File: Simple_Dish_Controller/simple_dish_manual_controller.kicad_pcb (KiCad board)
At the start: 4 copper layers, 65 x 75 mm, 50 parts, among them J1 Screw_Terminal_01x02, J2 Conn_01x02_Pin, J3 Screw Terminal To Chassis, J4 Conn_01x03_Pin, J5 Elevation DE-15, J6 Conn_01x03_Pin, J7 Azimuth DE-15, Q1 MMBT2222A, Q2 MMBT2222A, Q3 MMBT2222A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

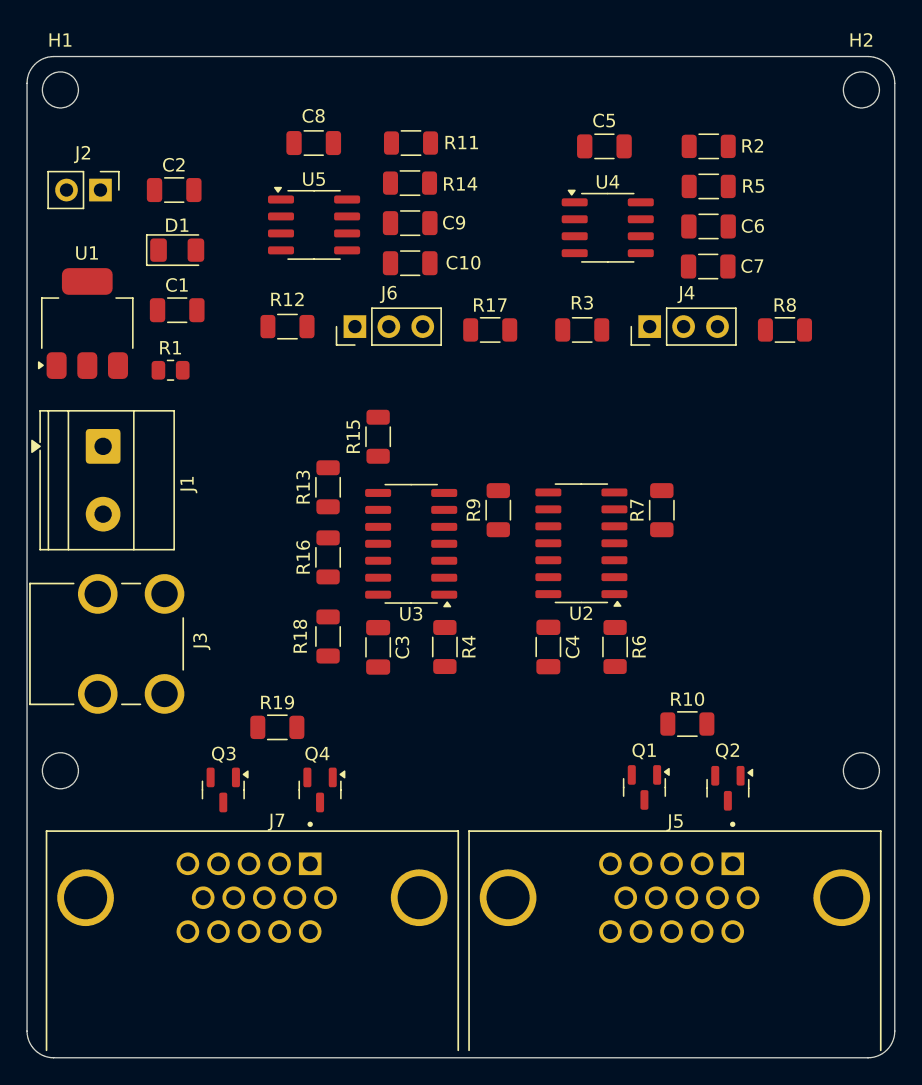
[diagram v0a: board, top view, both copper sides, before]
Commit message: Component placement and added traces
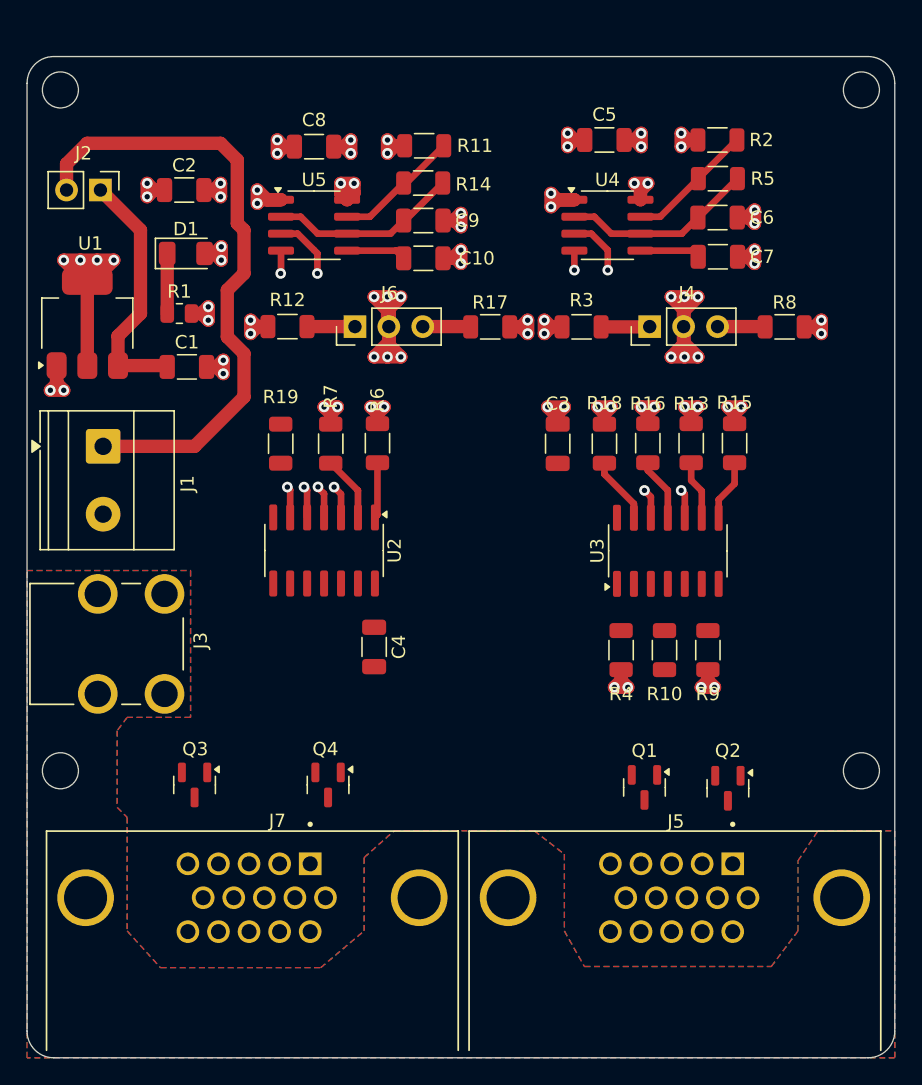
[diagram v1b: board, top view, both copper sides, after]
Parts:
- moved R13 27.4 mm to (220.2, 76.4)
- moved R15 26.7 mm to (223.5, 76.4)
- moved R16 25.4 mm to (217.0, 76.4)
- moved R7 25.3 mm to (193.2, 76.4)
- moved R18 25.2 mm to (213.8, 76.4), turned to 90 degrees
- moved R6 23.5 mm to (196.8, 76.4), turned to 90 degrees
- moved R19 21.3 mm to (189.5, 76.4), turned to -90 degrees
- moved C3 20.3 mm to (210.2, 76.4), turned to 90 degrees
- moved U2 19.3 mm to (192.8, 84.4), turned to -90 degrees
- moved U3 19.2 mm to (218.5, 84.4), turned to 90 degrees
- moved R9 18.9 mm to (221.5, 91.9), turned to -90 degrees
- moved R4 13.2 mm to (215.0, 91.9)
- moved C4 13.1 mm to (196.5, 91.6)
- moved R10 5.80 mm to (218.2, 91.9), turned to -90 degrees
- moved C1 4.31 mm to (182.5, 70.7)
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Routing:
- net GND: track 0.00 -> 89.8 mm, vias 0 -> 50
- net +5V: track 0.00 -> 84.8 mm, vias 0 -> 32
- net /IN_5VDC: track 0.00 -> 47.0 mm
- net /IN_5VDC_SWITCH: track 0.00 -> 18.8 mm
- net Net-(U4-THR): track 0.00 -> 14.4 mm
- net Net-(U5-THR): track 0.00 -> 14.2 mm
- net Net-(U4-DIS): track 0.00 -> 9.61 mm
- net Net-(U5-DIS): track 0.00 -> 9.44 mm
- net Net-(J6-Pin_3): track 0.00 -> 8.60 mm
- net Net-(R15-Pad1): track 0.00 -> 7.15 mm, vias 0 -> 1
- net Net-(R16-Pad1): track 0.00 -> 7.12 mm, vias 0 -> 1
- net /Azimuth/Dir Sig: track 0.00 -> 6.11 mm, vias 0 -> 1
- net Net-(R7-Pad1): track 0.00 -> 4.91 mm
- net /Azimuth/Pul sig: track 0.00 -> 4.84 mm, vias 0 -> 1
- net Net-(U4-CV): track 0.00 -> 4.52 mm
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- added copper zone on B.Cu, net Shield
- added copper zone on F.Cu, net Shield
- added copper zone on In1.Cu, net Shield
- added copper zone on In2.Cu, net Shield
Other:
- board text added: "25/04/2025"
- board text added: "DISH CONTROLLER"
- board text added: "HW 1.0.0"

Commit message: Final version of the PCB.Production files were generated in -Production- folder
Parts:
- C3, C4, C5, C8: value 0.1uF -> 100nF
- R1: footprint Resistor_SMD:R_0805_2012Metric -> Resistor_SMD:R_1206_3216Metric
- moved U3 5.21 mm to (213.3, 84.4)
- moved R10 4.94 mm to (213.3, 92.5)
- moved R4 4.94 mm to (210.1, 92.5)
- moved R9 4.94 mm to (216.6, 92.5)
- moved C3 3.55 mm to (206.7, 76.4)
- moved R13 3.55 mm to (216.7, 76.4)
- moved R15 3.55 mm to (219.9, 76.4)
- moved R16 3.55 mm to (213.4, 76.4)
- moved R18 3.55 mm to (210.2, 76.4)
- moved Q1 2.95 mm to (213.8, 102.2)
- moved Q2 1.30 mm to (224.3, 102.2)
- moved Q3 0.97 mm to (182.1, 102.2)
- moved C4 0.96 mm to (196.6, 92.6)
- moved R1 0.49 mm to (182.4, 66.6)
- moved Q4 0.40 mm to (192.7, 102.2)
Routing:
- net /Elevation/Pul sig: track 4.51 -> 60.5 mm, vias 1 -> 0
- net /Azimuth/Limit Sw1: track 4.45 -> 55.0 mm, vias 0 -> 2
- net /Elevation/Dir Sig: track 3.65 -> 52.6 mm, vias 0 -> 4
- net /Azimuth/Limit Sw2: track 2.25 -> 50.6 mm, vias 1 -> 2
- net /Azimuth/Pul sig: track 4.84 -> 47.9 mm, vias 1 -> 4
- net /Azimuth/Dir Sig: track 6.11 -> 45.6 mm, vias 1 -> 2
- net GND: track 89.8 -> 129.1 mm, vias 50 -> 68
- net Net-(R15-Pad1): track 7.15 -> 42.4 mm, vias 1 -> 2
- net /Elevation/Pulse Enable: track 3.95 -> 36.9 mm, vias 2 -> 0
- net /Elevation/Limit Sw1: track 0.00 -> 32.0 mm, vias 0 -> 1
- net Net-(R7-Pad1): track 4.91 -> 34.2 mm, vias 0 -> 2
- net Net-(J4-Pin_3): track 3.57 -> 31.9 mm
- net Net-(Q3-B): track 0.00 -> 27.3 mm
- net /Elevation/Limit Sw2: track 0.00 -> 26.6 mm
- net Net-(R16-Pad1): track 7.12 -> 32.1 mm, vias 1 -> 2
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- added copper zone on B.Cu, net GND
- added copper zone on F.Cu, net GND
